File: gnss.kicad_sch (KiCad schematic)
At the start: 69 parts, among them J11 Conn_Coaxial, J12 Conn_Coaxial_Small, Q12 AO3401A, Q13 BSS138, SW4 RESET_GNSS, SW5 SAFEBOOT_GNSS, U10 TPS7A2033PDBVR, U11 TPS259474LRPWR, U9 NEO-M9N

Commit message: change capacitor sizing & update footprints
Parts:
- R81: LCSC Part C49275310 -> C316909
- R87: footprint Resistor_SMD:R_0603_1608Metric_Pad0.98x0.95mm_HandSolder -> Resistor_SMD:R_0402_1005Metric_Pad0.72x0.64mm_HandSolder
- SW4, SW5: LCSC Part C2681476 -> C202388
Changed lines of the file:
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@@
 			)
 		)
-		(property "LCSC Part" "C2681476"
+		(property "LCSC Part" "C202388"
 			(at 90.17 92.71 0)
 			(hide yes)
@@
 			)
 		)
-		(property "Footprint" "Resistor_SMD:R_0603_1608Metric_Pad0.98x0.95mm_HandSolder"
+		(property "Footprint" "Resistor_SMD:R_0402_1005Metric_Pad0.72x0.64mm_HandSolder"
 			(at 204.47 45.72 0)
 			(hide yes)
@@
 			)
 		)
-		(property "LCSC Part" "C2681476"
+		(property "LCSC Part" "C202388"
 			(at 92.71 82.55 0)
 			(hide yes)
@@
 			)
 		)
-		(property "LCSC Part" "C49275310"
+		(property "LCSC Part" "C316909"
 			(at 130.81 149.86 0)
 			(hide yes)

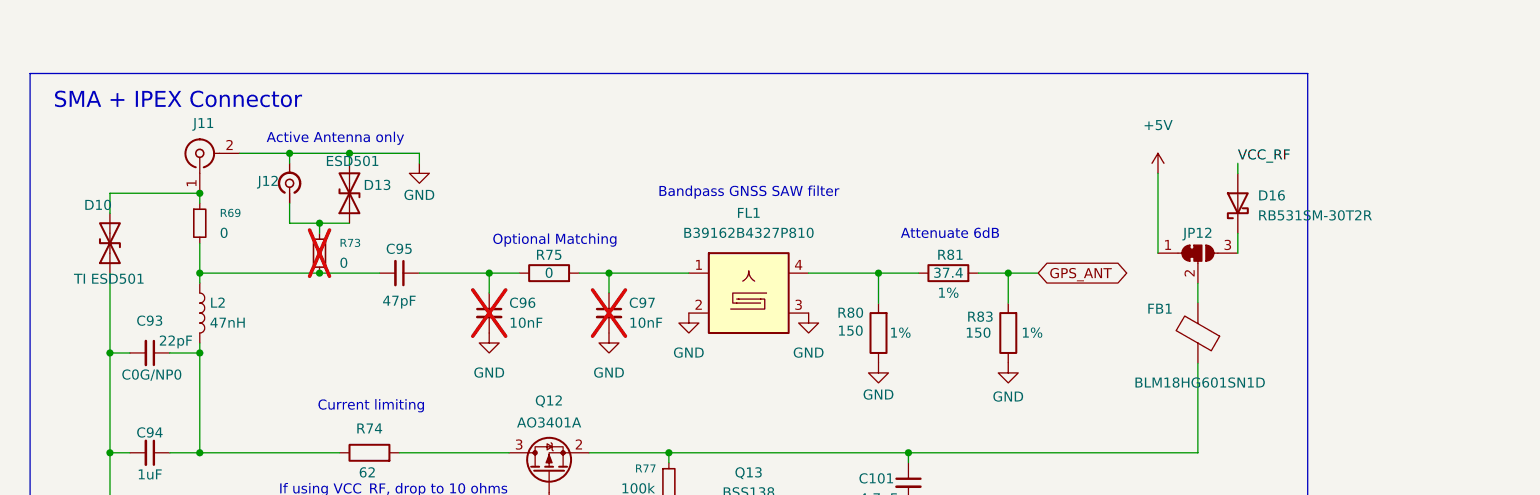
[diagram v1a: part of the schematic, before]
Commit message: small part renames in schematic + add step model
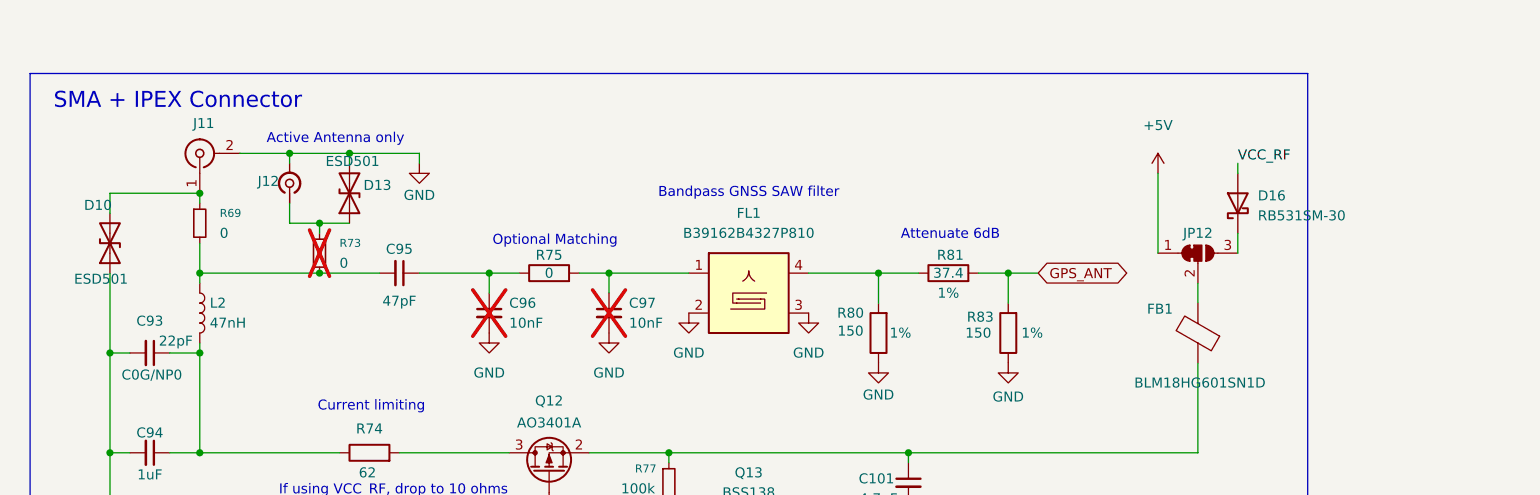
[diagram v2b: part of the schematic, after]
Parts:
- D10: value TI ESD501 -> ESD501
- D16: value RB531SM-30T2R -> RB531SM-30
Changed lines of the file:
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@@
 			)
 		)
-		(property "Value" "RB531SM-30T2R"
+		(property "Value" "RB531SM-30"
 			(at 170.18 142.5574 90)
 			(show_name no)
@@
 			)
 		)
-		(property "Value" "TI ESD501"
+		(property "Value" "ESD501"
 			(at 19.558 150.622 90)
 			(show_name no)

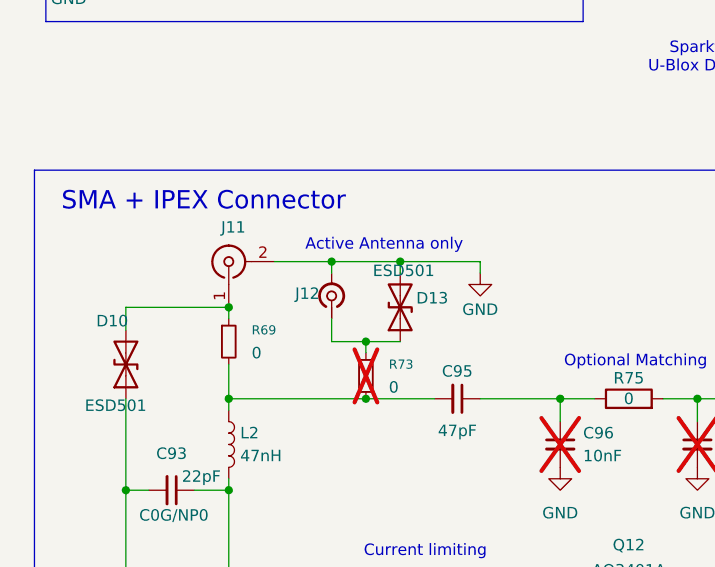
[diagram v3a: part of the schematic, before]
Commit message: assign lcsc part numbers
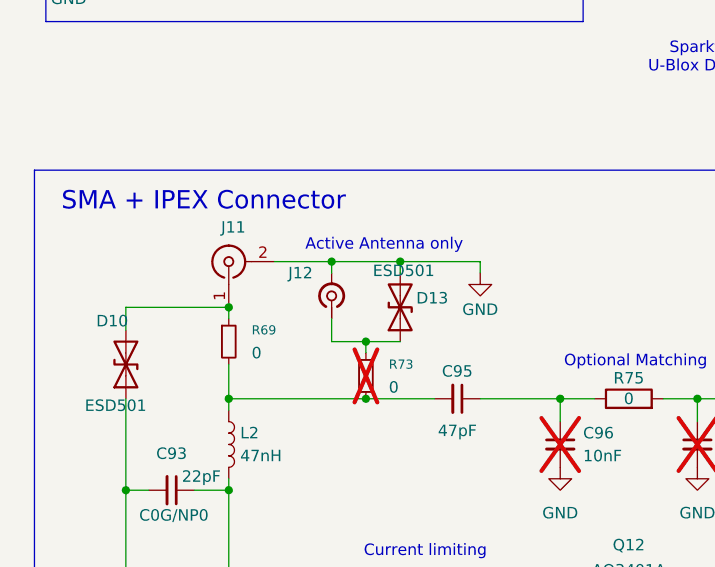
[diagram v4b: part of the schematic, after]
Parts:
- J11: LCSC Part (none) -> C5250058
- J12: LCSC Part (none) -> C88374
- R67, R76: LCSC Part C2902636 -> C54951138
- R71: LCSC Part (none) -> C48533754
- R88: LCSC Part (none) -> C49655648
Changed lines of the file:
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@@
 		(dnp no)
 		(property "Reference" "J12"
-			(at 42.926 138.176 90)
+			(at 42.164 135.89 90)
 			(show_name no)
 			(do_not_autoplace no)
@@
 			)
 		)
-		(property "LCSC Part" ""
+		(property "LCSC Part" "C88374"
 			(at 46.99 138.43 0)
 			(hide yes)
@@
 			)
 		)
+		(property "Capacitor Rating" ""
+			(at 46.99 138.43 0)
+			(hide yes)
+			(show_name no)
+			(do_not_autoplace no)
+			(effects
+				(font
+					(size 1.27 1.27)
+				)
+			)
+		)
 		(pin "1"
 		)
@@
 			)
 		)
-		(property "LCSC Part" "C2902636"
+		(property "LCSC Part" "C54951138"
 			(at 34.29 40.64 0)
 			(hide yes)
@@
 			)
 		)
-		(property "LCSC Part" "C2902636"
+		(property "LCSC Part" "C54951138"
 			(at 90.17 85.09 0)
 			(hide yes)
@@
 			)
 		)
-		(property "LCSC Part" ""
+		(property "LCSC Part" "C49655648"
 			(at 246.38 53.34 0)
 			(hide yes)
@@
 			)
 		)
-		(property "LCSC Part" ""
+		(property "LCSC Part" "C5250058"
 			(at 35.56 134.62 0)
 			(hide yes)
@@
 			)
 		)
+		(property "Capacitor Rating" ""
+			(at 35.56 134.62 0)
+			(hide yes)
+			(show_name no)
+			(do_not_autoplace no)
+			(effects
+				(font
+					(size 1.27 1.27)
+				)
+			)
+		)
 		(pin "2"
 		)
@@
 			)
 		)
-		(property "LCSC Part" ""
+		(property "LCSC Part" "C48533754"
 			(at 44.45 59.69 0)
 			(hide yes)

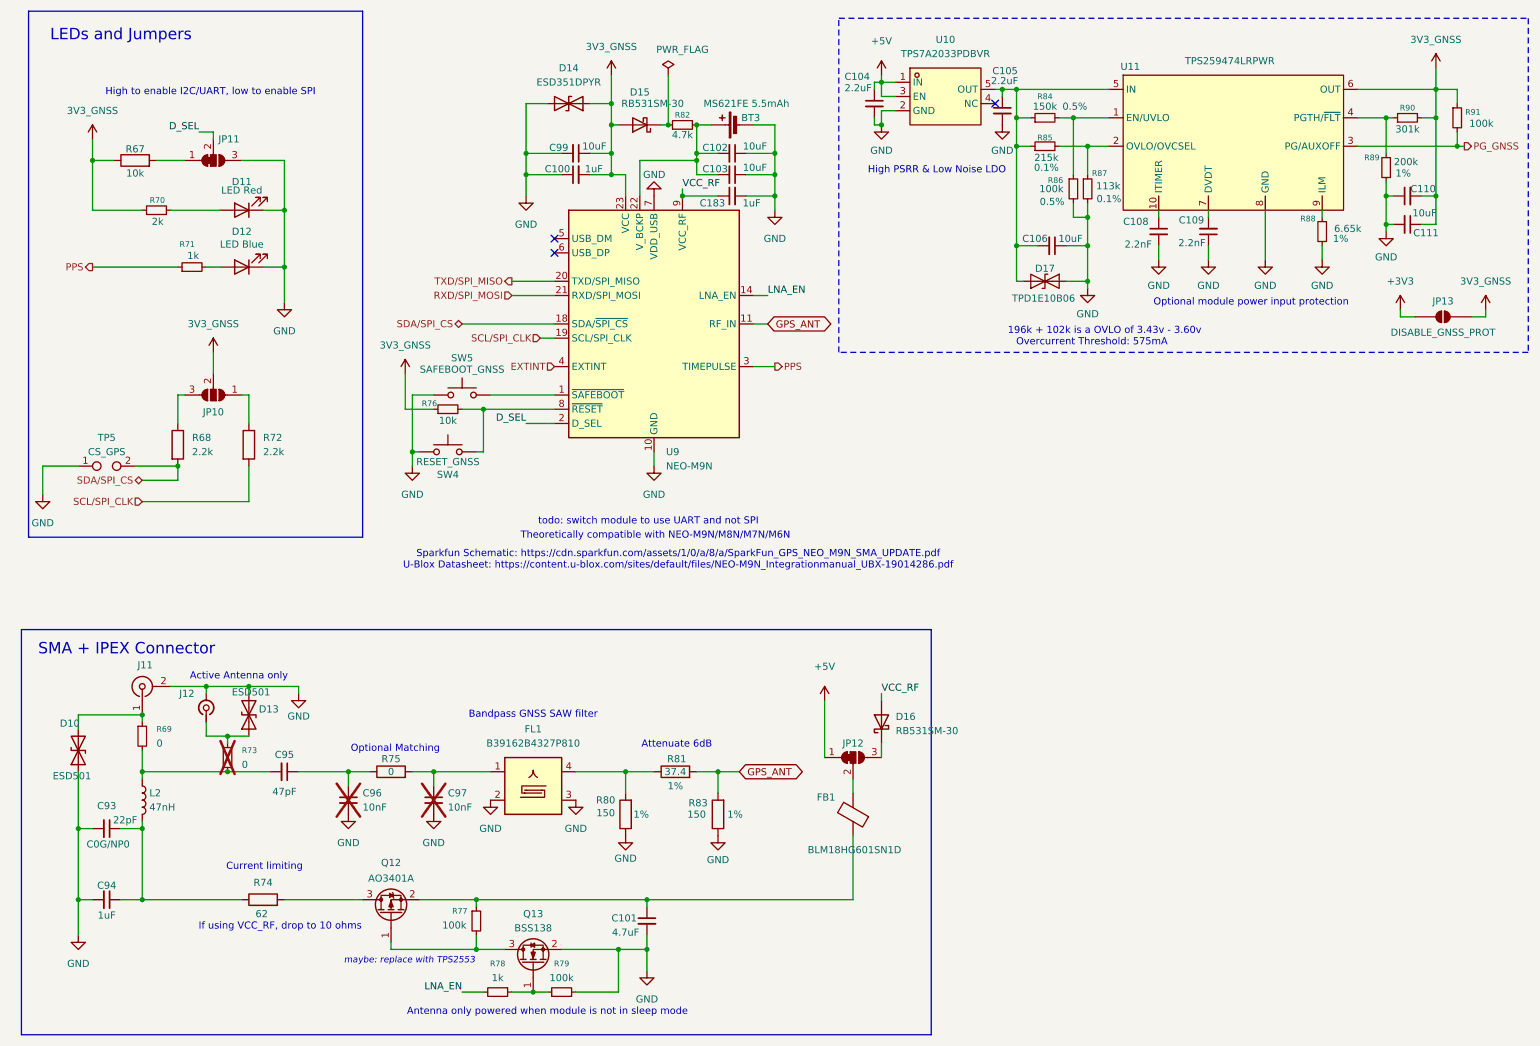
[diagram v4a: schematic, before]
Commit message: Update GNSS schematic to work with NEO-F10N by changing symbol & replacing SAW filter
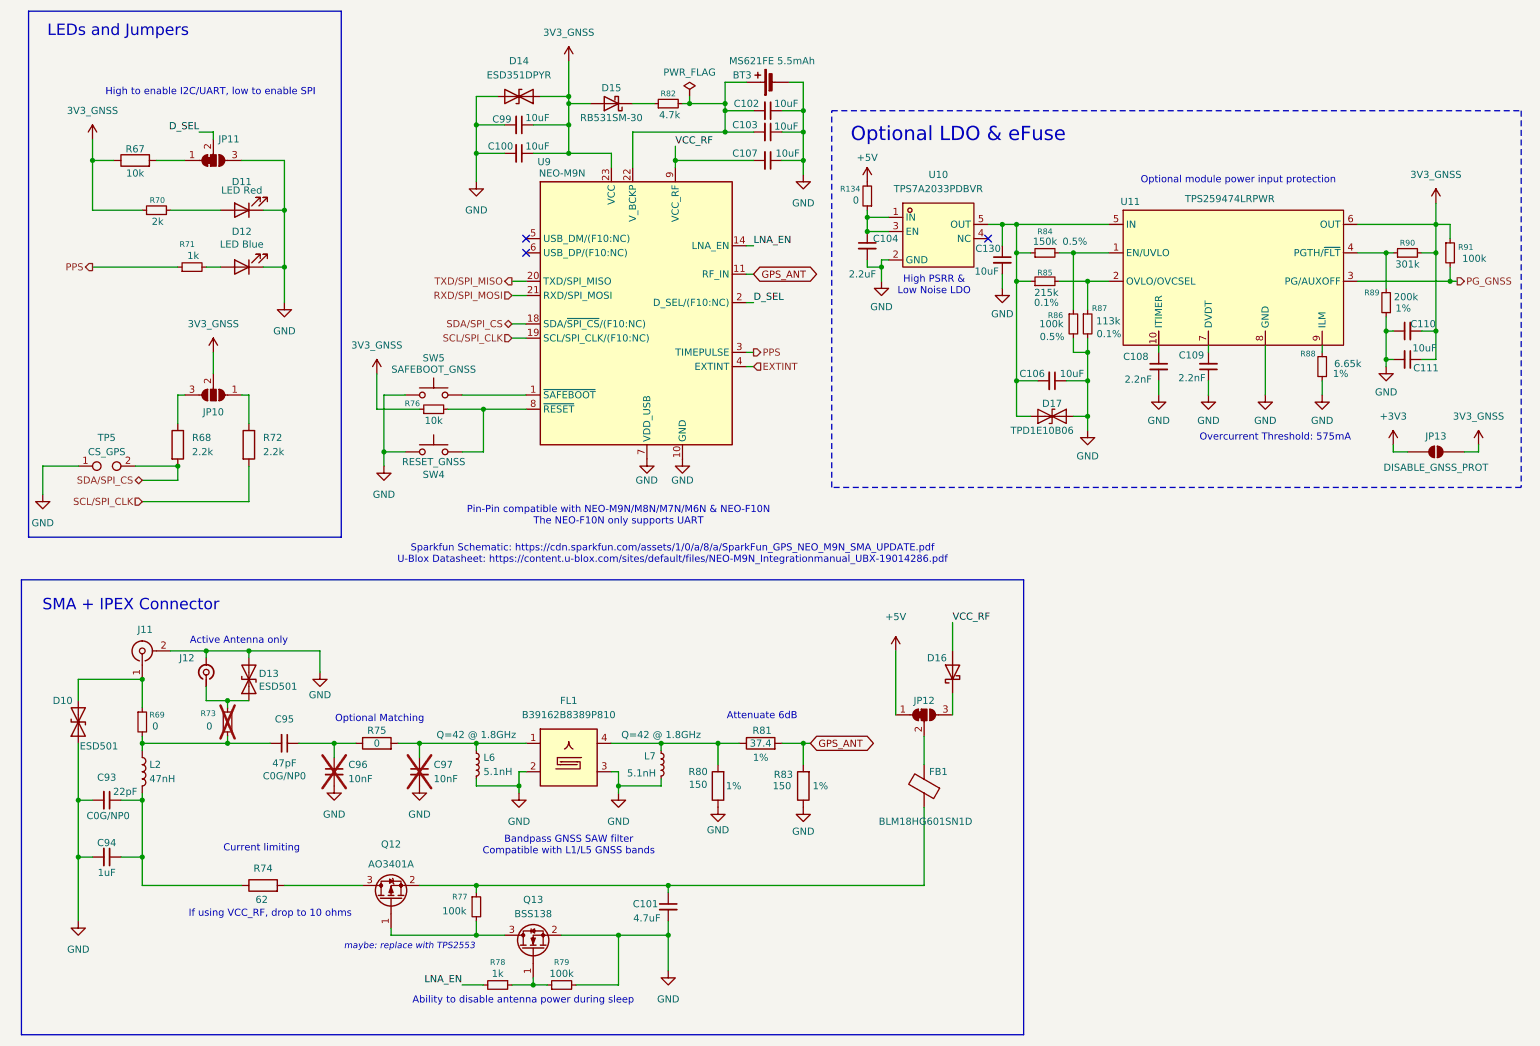
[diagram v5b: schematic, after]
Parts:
- removed C105: 2.2uF, Capacitor_SMD:C_0402_1005Metric, symbol Device:C_Small
- removed C183: 1uF, Capacitor_SMD:C_0402_1005Metric, symbol Device:C_Small
- added C107, C130: 10uF, Capacitor_SMD:C_0402_1005Metric, symbol Device:C_Small
- added L6, L7: 5.1nH, Inductor_SMD:L_0402_1005Metric, symbol Device:L_Small
- added R134: 0, Resistor_SMD:R_0402_1005Metric, symbol Device:R_Small
- C100: value 1uF -> 10uF; Capacitor Rating X7R -> (none); LCSC Part C53426846 -> C6119763; Voltage Rating 25V -> (none)
- C95: Capacitor Rating C0G -> C0G/NP0
- FL1: value B39162B4327P810 -> B39162B8389P810; LCSC Part C2650956 -> C5556161
- R73, U9: now left out of the parts list
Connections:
- net +5V: now also R134.2; no longer C104.1, U10.1 (IN), U10.3 (EN)
- net 3V3_GNSS: now also C100.1; no longer C100.2
- net GND: now also C100.2, C107.1, C130.2, L6.2, L7.2; no longer C100.1
- net VCC_RF: now also C107.2
- net at C106.2, D17.1 (A1), R84.1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: now also C130.1
- net at C97.1, FL1.1, R75.2: now also L6.1
- net at FL1.4, R80.2, R81.1: now also L7.1
- new net: C104.1, R134.1, U10.1 (IN), U10.3 (EN)
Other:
- note added: "Ability to disable antenna power during sleep"
- note added: "Bandpass GNSS SAW filter Compatible with L1/L5 GNSS bands"
- note added: "Optional LDO & eFuse"
- note added: "Pin-Pin compatible with NEO-M9N/M8N/M7N/M6N & NEO-F10N The NEO-F10N only supports UART"
- note removed: "196k + 102k is a OVLO of 3.43v - 3.60v"
- note removed: "Antenna only powered when module is not in sleep mode"
- note removed: "Bandpass GNSS SAW filter"
- note removed: "Theoretically compatible with NEO-M9N/M8N/M7N/M6N"
- note removed: "todo: switch module to use UART and not SPI"
- moved on the sheet: BT3, C101, C102, C103, C106, C108, C109, C110, C111, C93, C94, C95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
